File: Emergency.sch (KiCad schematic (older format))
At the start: 18 parts, among them J21 EMERGENCY, J22 EPSON POWER IN, J23 EPSON BOARD POWER, K1 S13-24V-2C, Q7 BC817, U8 74HC2G32

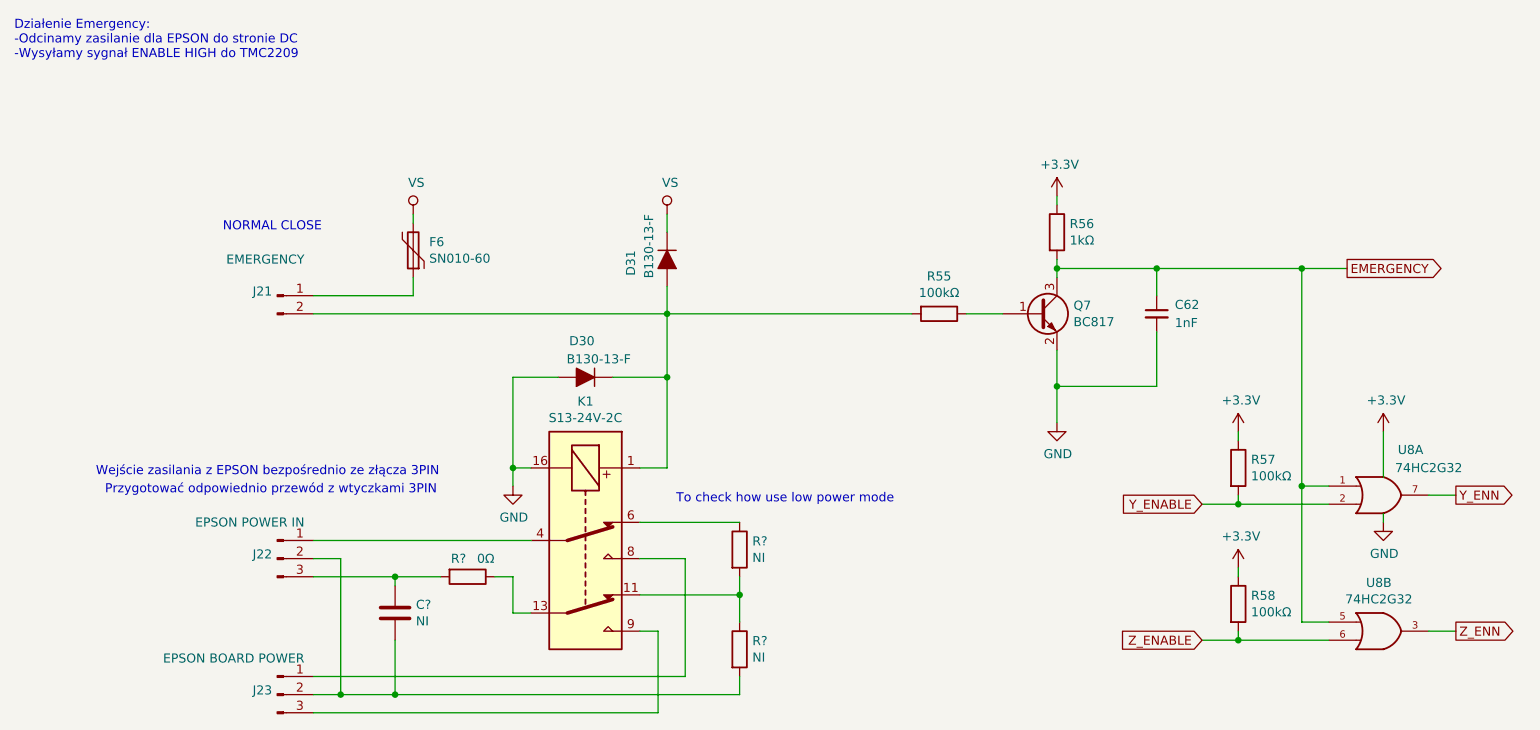
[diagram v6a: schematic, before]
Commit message: Added 12V regulator, aditional input, outputs, improved inputs ESD
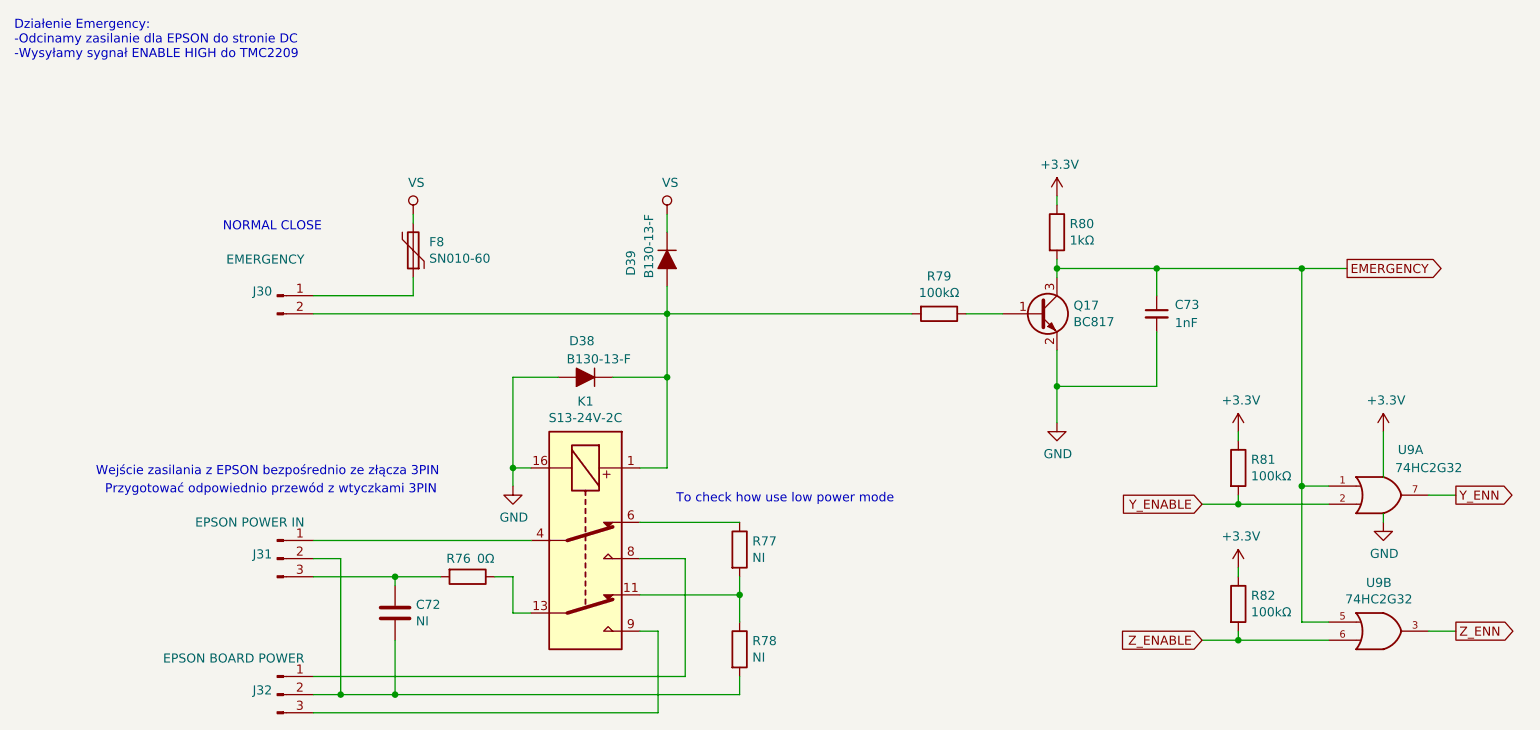
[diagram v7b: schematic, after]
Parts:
- gave numbers to parts that had none: 4
- renumbered C62 to C73, D30 to D38, D31 to D39, F6 to F8, J21 to J30, J22 to J31, J23 to J32, Q7 to Q17, R55 to R79, R56 to R80, R57 to R81, R58 to R82, U8 to U9
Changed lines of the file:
@@
 AR Path="/5E07245F/5E9227CA" Ref="J?"  Part="1"
 AR Path="/5E858220/5E9227CA" Ref="J?"  Part="1"
-AR Path="/5E91D7CC/5E9227CA" Ref="J22"  Part="1"
-F 0 "J22" H 2322 3724 50  0000 R CNN
+AR Path="/5E91D7CC/5E9227CA" Ref="J31"  Part="1"
+F 0 "J31" H 2322 3724 50  0000 R CNN
 F 1 "EPSON POWER IN" H 2500 3900 50  0000 R CNN
 F 2 "Connector_JST:JST_PH_B3B-PH-K_1x03_P2.00mm_Vertical" H 2350 3700 50  0001 C CNN
@@
 AR Path="/5E07245F/5E922904" Ref="J?"  Part="1"
 AR Path="/5E858220/5E922904" Ref="J?"  Part="1"
-AR Path="/5E91D7CC/5E922904" Ref="J23"  Part="1"
-F 0 "J23" H 2322 4474 50  0000 R CNN
+AR Path="/5E91D7CC/5E922904" Ref="J32"  Part="1"
+F 0 "J32" H 2322 4474 50  0000 R CNN
 F 1 "EPSON BOARD POWER" H 2500 4650 50  0000 R CNN
 F 2 "Connector_JST:JST_PH_B3B-PH-K_1x03_P2.00mm_Vertical" H 2350 4450 50  0001 C CNN
@@
 AR Path="/5E07245F/5E1228A3" Ref="J?"  Part="1"
 AR Path="/5E858220/5E1228A3" Ref="J?"  Part="1"
-AR Path="/5E91D7CC/5E1228A3" Ref="J21"  Part="1"
-F 0 "J21" H 2322 2274 50  0000 R CNN
+AR Path="/5E91D7CC/5E1228A3" Ref="J30"  Part="1"
+F 0 "J30" H 2322 2274 50  0000 R CNN
 F 1 "EMERGENCY" H 2500 2450 50  0000 R CNN
 F 2 "Connector_JST:JST_PH_B2B-PH-K_1x02_P2.00mm_Vertical" H 2350 2250 50  0001 C CNN
@@
 P 3100 1800
 AR Path="/5E1018C2/5E127E8D" Ref="#PWR?"  Part="1"
-AR Path="/5E91D7CC/5E127E8D" Ref="#PWR0139"  Part="1"
-F 0 "#PWR0139" H 2900 1650 50  0001 C CNN
+AR Path="/5E91D7CC/5E127E8D" Ref="#PWR0180"  Part="1"
+F 0 "#PWR0180" H 2900 1650 50  0001 C CNN
 F 1 "VS" H 3117 1973 50  0000 C CNN
 F 2 "" H 3100 1800 50  0001 C CNN
@@
 	4500 3200 4350 3200
 $Comp
-L power:GND #PWR0140
+L power:GND #PWR0181
 U 1 1 5E128738
 P 3650 3300
-F 0 "#PWR0140" H 3650 3050 50  0001 C CNN
+F 0 "#PWR0181" H 3650 3050 50  0001 C CNN
 F 1 "GND" H 3655 3127 50  0000 C CNN
 F 2 "" H 3650 3300 50  0001 C CNN
@@
 Connection ~ 3650 3200
 $Comp
-L Device:R R55
+L Device:R R79
 U 1 1 5E137914
 P 6000 2350
-F 0 "R55" V 5793 2350 50  0000 C CNN
+F 0 "R79" V 5793 2350 50  0000 C CNN
 F 1 "100kΩ" V 5884 2350 50  0000 C CNN
 F 2 "Resistor_SMD:R_0603_1608Metric" V 5930 2350 50  0001 C CNN
@@
 Connection ~ 4500 2350
 $Comp
-L Transistor_BJT:BC817 Q7
+L Transistor_BJT:BC817 Q17
 U 1 1 5E139012
 P 6550 2350
-F 0 "Q7" H 6741 2396 50  0000 L CNN
+F 0 "Q17" H 6741 2396 50  0000 L CNN
 F 1 "BC817" H 6741 2305 50  0000 L CNN
 F 2 "Package_TO_SOT_SMD:SOT-23" H 6750 2275 50  0001 L CIN
@@
 $EndComp
 $Comp
-L power:GND #PWR0143
+L power:GND #PWR0184
 U 1 1 5E13A402
 P 6650 2950
-F 0 "#PWR0143" H 6650 2700 50  0001 C CNN
+F 0 "#PWR0184" H 6650 2700 50  0001 C CNN
 F 1 "GND" H 6655 2777 50  0000 C CNN
 F 2 "" H 6650 2950 50  0001 C CNN
@@
 	6650 2550 6650 2750
 $Comp
-L Device:R R56
+L Device:R R80
 U 1 1 5E13AACA
 P 6650 1900
-F 0 "R56" H 6720 1946 50  0000 L CNN
+F 0 "R80" H 6720 1946 50  0000 L CNN
 F 1 "1kΩ" H 6720 1855 50  0000 L CNN
 F 2 "Resistor_SMD:R_0603_1608Metric" V 6580 1900 50  0001 C CNN
@@
 	6650 1700 6650 1750
 $Comp
-L power:+3.3V #PWR0142
+L power:+3.3V #PWR0183
 U 1 1 5E13B5C9
 P 6650 1700
-F 0 "#PWR0142" H 6650 1550 50  0001 C CNN
+F 0 "#PWR0183" H 6650 1550 50  0001 C CNN
 F 1 "+3.3V" H 6665 1873 50  0000 C CNN
 F 2 "" H 6650 1700 50  0001 C CNN
@@
 $EndComp
 $Comp
-L Library:74HC2G32 U8
+L Library:74HC2G32 U9
 U 1 1 5E1329B6
 P 8450 3350
-F 0 "U8" H 8600 3600 50  0000 C CNN
+F 0 "U9" H 8600 3600 50  0000 C CNN
 F 1 "74HC2G32" H 8700 3500 50  0000 C CNN
 F 2 "Package_SO:VSSOP-8_2.3x2mm_P0.5mm" H 8450 3350 50  0001 C CNN
@@
 $EndComp
 $Comp
-L Library:74HC2G32 U8
+L Library:74HC2G32 U9
 U 2 1 5E133AA3
 P 8450 4100
-F 0 "U8" H 8425 4367 50  0000 C CNN
+F 0 "U9" H 8425 4367 50  0000 C CNN
 F 1 "74HC2G32" H 8425 4276 50  0000 C CNN
 F 2 "Package_SO:VSSOP-8_2.3x2mm_P0.5mm" H 8450 4100 50  0001 C CNN
@@
 $EndComp
 $Comp
-L power:GND #PWR0147
+L power:GND #PWR0188
 U 1 1 5E136188
 P 8450 3500
-F 0 "#PWR0147" H 8450 3250 50  0001 C CNN
+F 0 "#PWR0188" H 8450 3250 50  0001 C CNN
 F 1 "GND" H 8455 3327 50  0000 C CNN
 F 2 "" H 8450 3500 50  0001 C CNN
@@
 $EndComp
 $Comp
-L power:+3.3V #PWR0146
+L power:+3.3V #PWR0187
 U 1 1 5E13670F
 P 8450 3000
-F 0 "#PWR0146" H 8450 2850 50  0001 C CNN
+F 0 "#PWR0187" H 8450 2850 50  0001 C CNN
 F 1 "+3.3V" H 8465 3173 50  0000 C CNN
 F 2 "" H 8450 3000 50  0001 C CNN
@@
 	7450 4150 7650 4150
 $Comp
-L Device:R R58
+L Device:R R82
 U 1 1 5E14A9EB
 P 7650 3950
-F 0 "R58" H 7720 3996 50  0000 L CNN
+F 0 "R82" H 7720 3996 50  0000 L CNN
 F 1 "100kΩ" H 7720 3905 50  0000 L CNN
 F 2 "Resistor_SMD:R_0603_1608Metric" V 7580 3950 50  0001 C CNN
@@
 	6650 2100 6650 2150
 $Comp
-L Device:R R57
+L Device:R R81
 U 1 1 5E14F006
 P 7650 3200
-F 0 "R57" H 7720 3246 50  0000 L CNN
+F 0 "R81" H 7720 3246 50  0000 L CNN
 F 1 "100kΩ" H 7720 3155 50  0000 L CNN
 F 2 "Resistor_SMD:R_0603_1608Metric" V 7580 3200 50  0001 C CNN
@@
 	7650 3400 7450 3400
 $Comp
-L power:+3.3V #PWR0144
+L power:+3.3V #PWR0185
 U 1 1 5E151EAA
 P 7650 3000
-F 0 "#PWR0144" H 7650 2850 50  0001 C CNN
+F 0 "#PWR0185" H 7650 2850 50  0001 C CNN
 F 1 "+3.3V" H 7665 3173 50  0000 C CNN
 F 2 "" H 7650 3000 50  0001 C CNN
@@
 $EndComp
 $Comp
-L power:+3.3V #PWR0145
+L power:+3.3V #PWR0186
 U 1 1 5E152501
 P 7650 3750
-F 0 "#PWR0145" H 7650 3600 50  0001 C CNN
+F 0 "#PWR0186" H 7650 3600 50  0001 C CNN
 F 1 "+3.3V" H 7665 3923 50  0000 C CNN
 F 2 "" H 7650 3750 50  0001 C CNN
@@
 P 3100 2000
 AR Path="/5E07245F/5E164594" Ref="F?"  Part="1"
-AR Path="/5E91D7CC/5E164594" Ref="F6"  Part="1"
-F 0 "F6" H 3012 1954 50  0000 R CNN
+AR Path="/5E91D7CC/5E164594" Ref="F8"  Part="1"
+F 0 "F8" H 3012 1954 50  0000 R CNN
 F 1 "SN010-60 " H 3012 2045 50  0000 R CNN
 F 2 "Fuse:Fuse_1206_3216Metric" H 3150 1800 50  0001 L CNN
@@
 AR Path="/5DE588DC/5E16709A" Ref="C?"  Part="1"
 AR Path="/5E1018C2/5E16709A" Ref="C?"  Part="1"
-AR Path="/5E91D7CC/5E16709A" Ref="C62"  Part="1"
-F 0 "C62" H 7300 2400 50  0000 L CNN
+AR Path="/5E91D7CC/5E16709A" Ref="C73"  Part="1"
+F 0 "C73" H 7300 2400 50  0000 L CNN
 F 1 "1nF" H 7300 2300 50  0000 L CNN
 F 2 "Capacitor_SMD:C_0603_1608Metric" H 7200 2350 50  0001 C CNN
@@
 P 4050 2700
 AR Path="/5E1018C2/5E199862" Ref="D?"  Part="1"
-AR Path="/5E91D7CC/5E199862" Ref="D30"  Part="1"
-F 0 "D30" H 4000 2500 50  0000 L CNN
+AR Path="/5E91D7CC/5E199862" Ref="D38"  Part="1"
+F 0 "D38" H 4000 2500 50  0000 L CNN
 F 1 "B130-13-F" H 3800 2600 50  0000 L CNN
 F 2 "Diode_SMD:D_SMA" H 4050 2700 50  0001 C CNN
@@
 P 4500 2050
 AR Path="/5E1018C2/5E28E0C0" Ref="D?"  Part="1"
-AR Path="/5E91D7CC/5E28E0C0" Ref="D31"  Part="1"
-F 0 "D31" H 4450 1850 50  0000 L CNN
+AR Path="/5E91D7CC/5E28E0C0" Ref="D39"  Part="1"
+F 0 "D39" H 4450 1850 50  0000 L CNN
 F 1 "B130-13-F" H 4250 1950 50  0000 L CNN
 F 2 "Diode_SMD:D_SMA" H 4500 2050 50  0001 C CNN
@@
 P 4500 1800
 AR Path="/5E1018C2/5E28EAC8" Ref="#PWR?"  Part="1"
-AR Path="/5E91D7CC/5E28EAC8" Ref="#PWR0141"  Part="1"
-F 0 "#PWR0141" H 4300 1650 50  0001 C CNN
+AR Path="/5E91D7CC/5E28EAC8" Ref="#PWR0182"  Part="1"
+F 0 "#PWR0182" H 4300 1650 50  0001 C CNN
 F 1 "VS" H 4517 1973 50  0000 C CNN
 F 2 "" H 4500 1800 50  0001 C CNN
@@
 	4500 2200 4500 2350
 $Comp
-L Device:R R?
+L Device:R R77
 U 1 1 5E291C98
 P 4900 3650
-F 0 "R?" H 4970 3696 50  0000 L CNN
+F 0 "R77" H 4970 3696 50  0000 L CNN
 F 1 "NI" H 4970 3605 50  0000 L CNN
 F 2 "Resistor_SMD:R_0805_2012Metric" V 4830 3650 50  0001 C CNN
@@
 $EndComp
 $Comp
-L Device:R R?
+L Device:R R78
 U 1 1 5E292A48
 P 4900 4200
-F 0 "R?" H 4970 4246 50  0000 L CNN
+F 0 "R78" H 4970 4246 50  0000 L CNN
 F 1 "NI" H 4970 4155 50  0000 L CNN
 F 2 "Resistor_SMD:R_0805_2012Metric" V 4830 4200 50  0001 C CNN
@@
 To check how use low power mode
 $Comp
-L Device:R R?
+L Device:R R76
 U 1 1 5E297579
 P 3400 3800
-F 0 "R?" V 3300 3750 50  0000 C CNN
+F 0 "R76" V 3300 3750 50  0000 C CNN
 F 1 "0Ω" V 3300 3900 50  0000 C CNN
 F 2 "Resistor_SMD:R_0805_2012Metric" V 3330 3800 50  0001 C CNN
@@
 	3550 3800 3650 3800
 $Comp
-L Device:C C?
+L Device:C C72
 U 1 1 5E299010
 P 3000 4000
-F 0 "C?" H 3115 4046 50  0000 L CNN
+F 0 "C72" H 3115 4046 50  0000 L CNN
 F 1 "NI" H 3115 3955 50  0000 L CNN
 F 2 "Capacitor_SMD:C_0805_2012Metric" H 3038 3850 50  0001 C CNN

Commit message: Added analog input
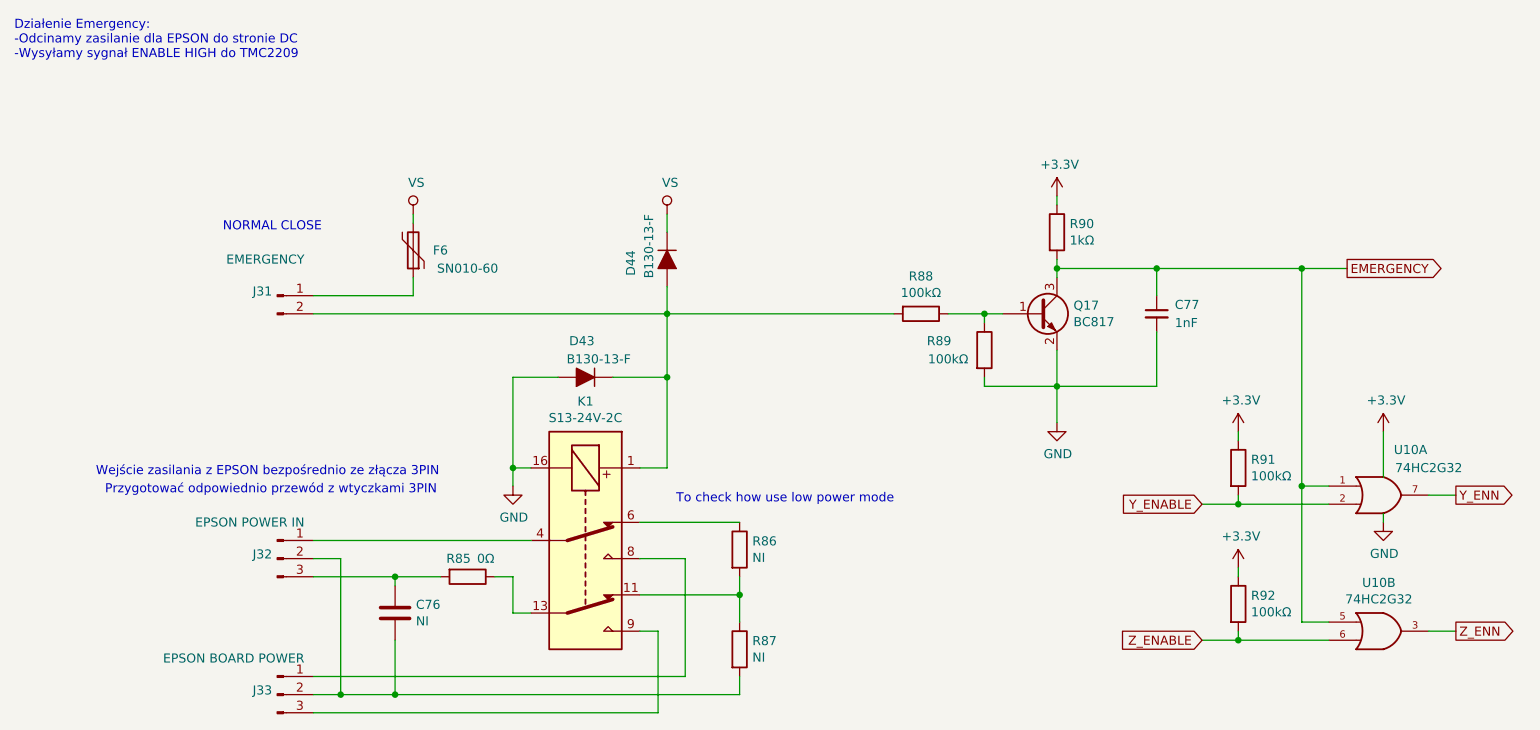
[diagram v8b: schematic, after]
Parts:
- removed F8: SN010-60, Fuse:Fuse_1206_3216Metric, symbol Device:Polyfuse
- added F6: SN010-60, Fuse:Fuse_1206_3216Metric, symbol Device:Polyfuse
- added R89: 100kΩ, Resistor_SMD:R_0603_1608Metric, symbol Device:R
- renumbered C72 to C76, C73 to C77, D38 to D43, D39 to D44, J30 to J31, J31 to J32, J32 to J33, R76 to R85, R77 to R86, R78 to R87, R79 to R88, R80 to R90, R81 to R91, R82 to R92, U9 to U10
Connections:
- net GND: now also R89.2
- net VS: now also F6.2
- net at J31.1 (Pin_1): now also F6.1
- net at Q17.1 (B), R88.1: now also R89.1
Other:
- moved on the sheet: R88
